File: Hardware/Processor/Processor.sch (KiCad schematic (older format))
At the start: 101 parts, among them J1 5V, J2 UART0, J3 USB_OTG, J4 JTAGICE3-SWD, J5 PIOA, J6 PIOB, J7 PIOC, J8 PIOD, Q1 BSSB06NE, Q2 BSSB06NE, Q3 BSSB06NE, Q4 BSSB06NE, SW1 PB, SW2 PB, SW3 ~RST, U1 TXS0102, U2 ATSAM4E16E, U3 3.0V, U4 LM3671, U5 PRTR5V0U2X, Y1 32.768kHz, Y2 12MHz

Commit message: Added note
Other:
- note added: "Remove local KiCad Libs from past projects"
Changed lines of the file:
@@
 LIBS:valves
 LIBS:common
+LIBS:newFritzLib
 LIBS:Processor-cache
 EELAYER 26 0
@@
 Wire Wire Line
 	9225 9125 9225 9100
+Text Notes 1450 -325 0    394  ~ 0
+Remove local KiCad Libs from past projects
 $EndSCHEMATC

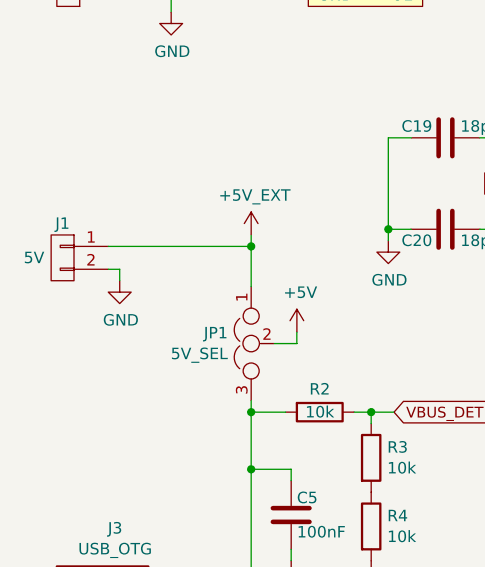
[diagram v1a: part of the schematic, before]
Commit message: Added extra pin to J1 connector to make it surface mount, BOM Complete except for xtals.
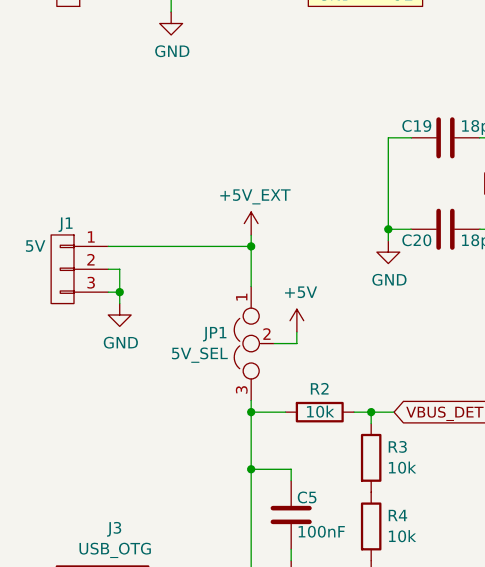
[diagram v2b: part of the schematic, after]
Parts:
- removed J1: 5V, symbol CONN_01X02
- added J1: 5V, symbol CONN_01X03
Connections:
- net +5V_EXT: now also J1.1 (P1)
- net GND: now also J1.2 (P2), J1.3 (P3)
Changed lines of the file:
@@
-$EndComp
-$Comp
-L CONN_01X02 J1
-U 1 1 58AC4E21
-P 925 6875
-F 0 "J1" H 925 7025 50  0000 C CNN
-F 1 "5V" H 1050 6875 50  0000 C CNN
-F 2 "" H -525 -575 50  0001 C CNN
-F 3 "" H -525 -575 50  0001 C CNN
-	1    925  6875
-	-1   0    0    -1
 $EndComp
 $Comp
 L GND #PWR057
 U 1 1 58AC6385
-P 1175 6975
-F 0 "#PWR057" H -875 -75 50  0001 C CNN
-F 1 "GND" H 1180 6802 50  0000 C CNN
-F 2 "" H -875 175 50  0001 C CNN
-F 3 "" H -875 175 50  0001 C CNN
-	1    1175 6975
+P 1175 7075
+F 0 "#PWR057" H -875 25  50  0001 C CNN
+F 1 "GND" H 1180 6902 50  0000 C CNN
+F 2 "" H -875 275 50  0001 C CNN
+F 3 "" H -875 275 50  0001 C CNN
+	1    1175 7075
 	1    0    0    -1
 $EndComp
@@
 	1125 6925 1175 6925
 Wire Wire Line
-	1175 6925 1175 6975
+	1175 6925 1175 7075
 Wire Wire Line
 	1125 6825 1750 6825
@@
 Text Notes 1450 -325 0    394  ~ 0
 Remove local KiCad Libs from past projects
+$Comp
+L CONN_01X03 J1
+U 1 1 58A68985
+P 925 6925
+F 0 "J1" H 875 7125 50  0000 L CNN
+F 1 "5V" H 1000 7025 50  0000 L CNN
+F 2 "" H 75  -300 50  0001 C CNN
+F 3 "" H 75  -300 50  0001 C CNN
+	1    925  6925
+	-1   0    0    -1
+$EndComp
+Wire Wire Line
+	1175 7025 1125 7025
+Connection ~ 1175 7025
 $EndSCHEMATC

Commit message: Fixed some autosave issues
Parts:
- C1, C10, C11, C12, C13, C14, C15, C16, C17, C18, C19, C2, C20, C21, C22, C23, C24, C25, C26, C27, C28, C29, C3, C30, C32, C33, C36, C37, C38, C39, C4, C5, C6, C7, C8, C9, R1, R10, R11, R12, R13, R15, R16, R18, R2, R20, R3, R4, R5, R6, R7, R8, R9: footprint (none) -> Capacitors_SMD:C_0603
- C31, C34, C35, C40, C41, R14, R17, R19, R21, R22: footprint (none) -> Capacitors_SMD:C_0805
- D1, D2, D3, D4, D5: footprint (none) -> LEDs:LED_0805
- J3: footprint (none) -> FritzLib:conn_usb_B_micro_smd
- J5, J7, J8: footprint (none) -> FritzLib:ConnectorSMD-40
- J6: footprint (none) -> FritzLib:ConnectorSMD-24
- SW1, SW2, SW3: footprint (none) -> Buttons_Switches_SMD:SW_SPST_TL3342
- TP1, TP2, TP3, TP4, TP5, TP6, TP7, TP8: footprint (none) -> Measurement_Points:Measurement_Point_Round-SMD-Pad_Small
- U2: footprint (none) -> Housings_QFP:TQFP-144_20x20mm_Pitch0.5mm

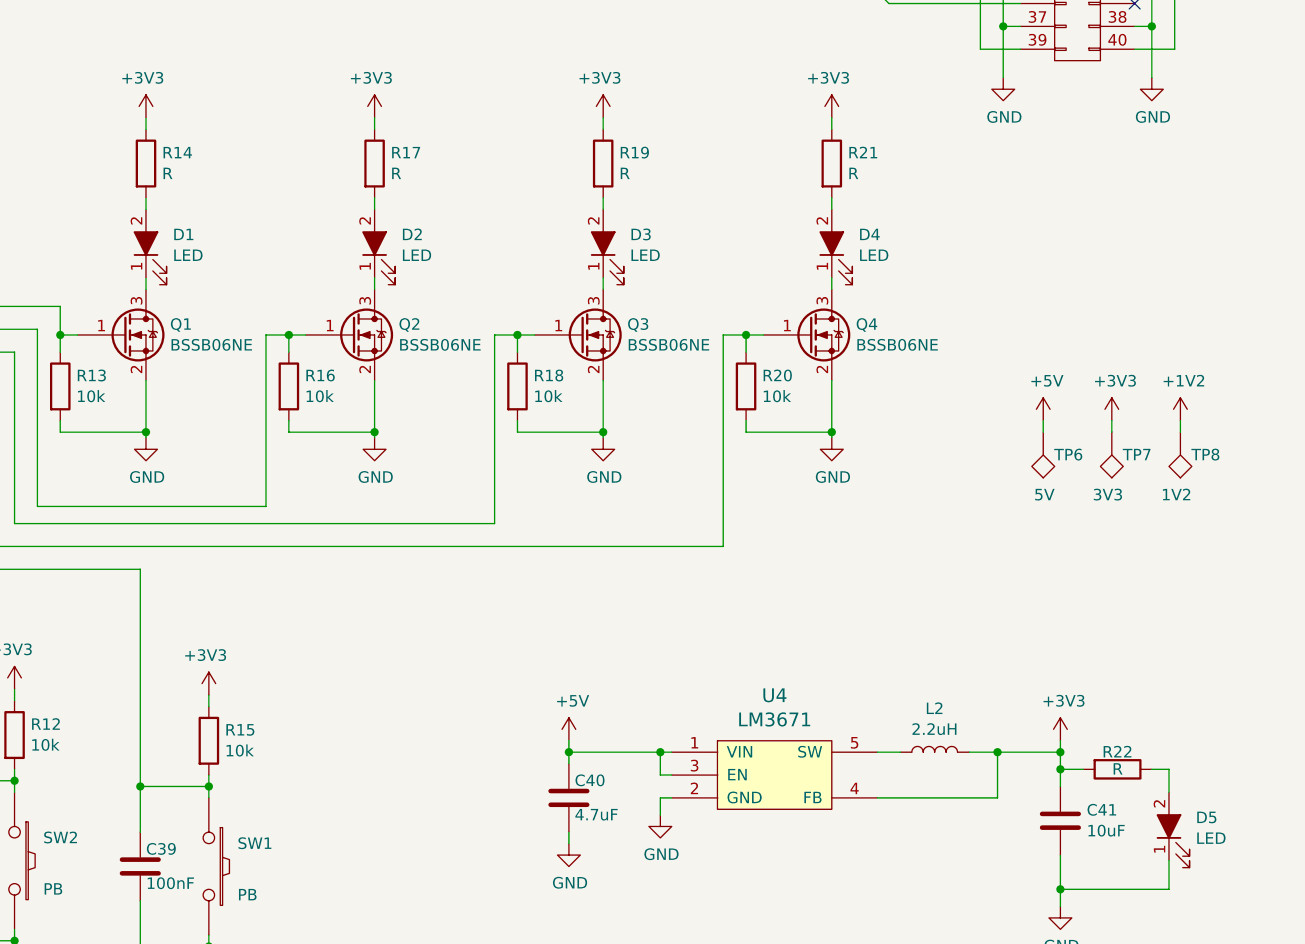
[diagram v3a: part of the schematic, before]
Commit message: Assigned proper value to current limiting resistors for LEDs, fixed autosave file
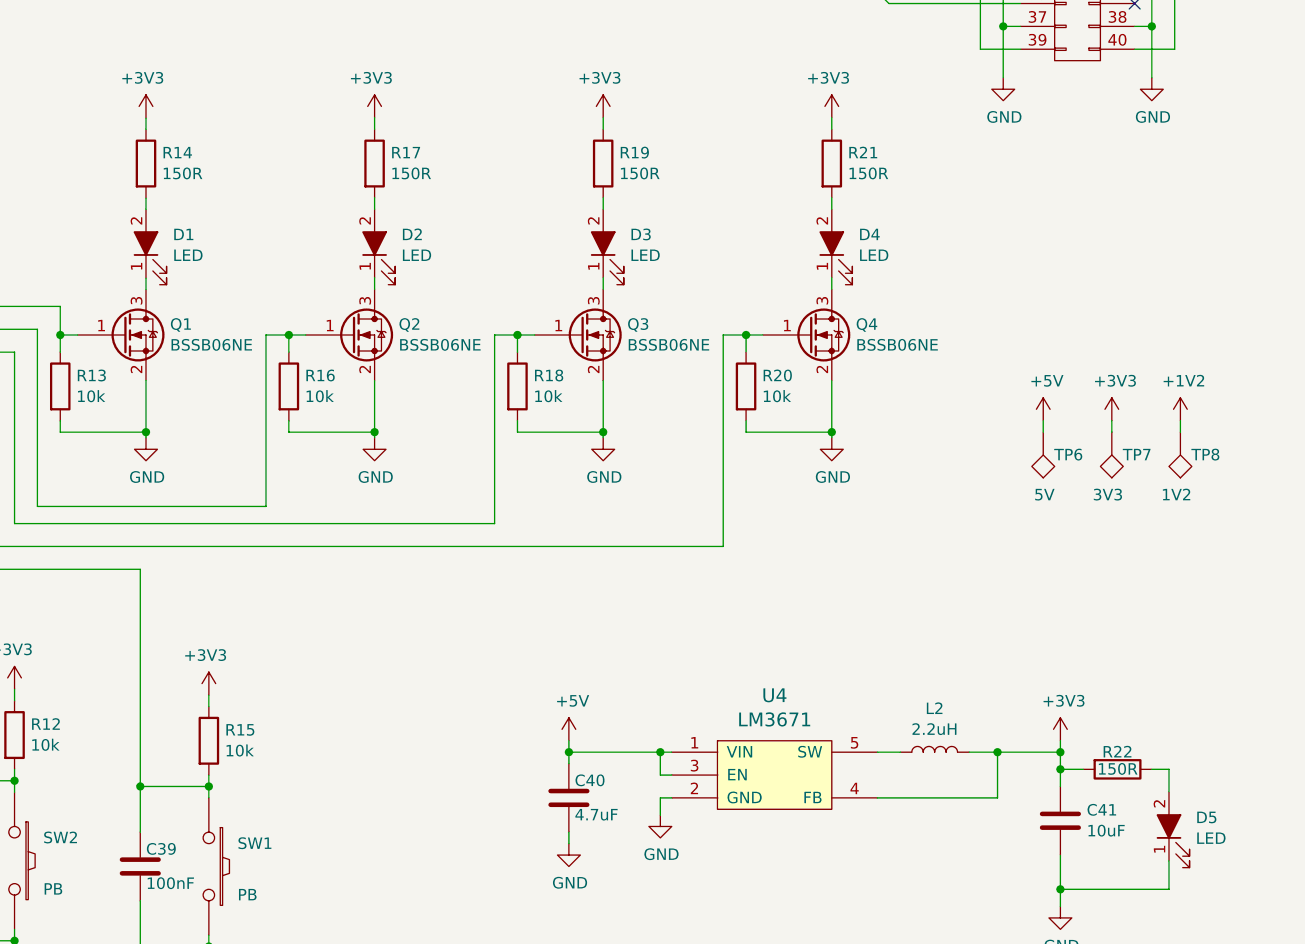
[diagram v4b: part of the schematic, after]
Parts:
- R14, R17, R19, R21, R22: value R -> 150R
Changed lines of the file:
@@
 P 10800 6725
 F 0 "R14" H 10870 6771 50  0000 L CNN
-F 1 "R" H 10870 6680 50  0000 L CNN
+F 1 "150R" H 10870 6680 50  0000 L CNN
 F 2 "Capacitors_SMD:C_0805" V 2705 4775 50  0001 C CNN
 F 3 "" H 2775 4775 50  0001 C CNN
@@
 P 15050 9375
 F 0 "R22" V 14975 9375 50  0000 C CNN
-F 1 "R" V 15050 9375 50  0000 C CNN
+F 1 "150R" V 15050 9375 50  0000 C CNN
 F 2 "Capacitors_SMD:C_0805" V 6955 7425 50  0001 C CNN
 F 3 "" H 7025 7425 50  0001 C CNN
@@
 P 11800 6725
 F 0 "R17" H 11870 6771 50  0000 L CNN
-F 1 "R" H 11870 6680 50  0000 L CNN
+F 1 "150R" H 11870 6680 50  0000 L CNN
 F 2 "Capacitors_SMD:C_0805" V 3705 4775 50  0001 C CNN
 F 3 "" H 3775 4775 50  0001 C CNN
@@
 P 12800 6725
 F 0 "R19" H 12870 6771 50  0000 L CNN
-F 1 "R" H 12870 6680 50  0000 L CNN
+F 1 "150R" H 12870 6680 50  0000 L CNN
 F 2 "Capacitors_SMD:C_0805" V 4705 4775 50  0001 C CNN
 F 3 "" H 4775 4775 50  0001 C CNN
@@
 P 13800 6725
 F 0 "R21" H 13870 6771 50  0000 L CNN
-F 1 "R" H 13870 6680 50  0000 L CNN
+F 1 "150R" H 13870 6680 50  0000 L CNN
 F 2 "Capacitors_SMD:C_0805" V 5705 4775 50  0001 C CNN
 F 3 "" H 5775 4775 50  0001 C CNN

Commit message: Updated BOM & Netlist. Started PCB Layout
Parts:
- J1, JP1: footprint (none) -> FritzLib:ConnectorSMD-1x3
- J2: footprint (none) -> FritzLib:ConnectorSMD-1x4
- J4: footprint (none) -> FritzLib:ConnectorMicromatch-10
- L1: footprint (none) -> FritzLib:Inductor_3mmx3mm
- L2: footprint (none) -> Inductors:Inductor_1212
- Q1, Q2, Q3, Q4, U3: footprint (none) -> TO_SOT_Packages_SMD:SOT-23
- U1: footprint (none) -> Housings_SSOP:MSOP-8_3x3mm_Pitch0.65mm
- U4: footprint (none) -> TO_SOT_Packages_SMD:SOT-23-5
- U5: footprint (none) -> FritzLib:SOT143B
- Y1: footprint (none) -> FritzLib:FC-135R
- Y2: footprint (none) -> Crystals:Crystal_HC49-SD_SMD
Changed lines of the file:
@@
 F 0 "L2" V 14440 9300 50  0000 C CNN
 F 1 "2.2uH" V 14349 9300 50  0000 C CNN
-F 2 "" H 4000 4725 50  0001 C CNN
+F 2 "Inductors:Inductor_1212" H 4000 4725 50  0001 C CNN
 F 3 "" H 4000 4725 50  0001 C CNN
 	1    14250 9300
@@
 F 0 "L1" H 5984 1704 50  0000 R CNN
 F 1 "10uH" H 5984 1795 50  0000 R CNN
-F 2 "" H -4225 -2825 50  0001 C CNN
+F 2 "FritzLib:Inductor_3mmx3mm" H -4225 -2825 50  0001 C CNN
 F 3 "" H -4225 -2825 50  0001 C CNN
 	1    6025 1750
@@
 F 0 "U3" V 7054 2554 50  0000 L CNN
 F 1 "3.0V" V 7145 2554 50  0000 L CNN
-F 2 "" H -4025 100 50  0001 C CNN
+F 2 "TO_SOT_Packages_SMD:SOT-23" H -4025 100 50  0001 C CNN
 F 3 "" H -4025 100 50  0001 C CNN
 F 4 "LM4040C30" V 7100 2475 60  0001 C CNN "MFG#"
@@
 F 0 "J4" H 10100 2665 50  0000 C CNN
 F 1 "JTAGICE3-SWD" H 10100 2574 50  0000 C CNN
-F 2 "" H -3175 -3425 50  0001 C CNN
+F 2 "FritzLib:ConnectorMicromatch-10" H -3175 -3425 50  0001 C CNN
 F 3 "" H -3175 -3425 50  0001 C CNN
 	1    10100 2250
@@
 F 0 "U4" H 13550 9847 60  0000 C CNN
 F 1 "LM3671" H 13550 9741 60  0000 C CNN
-F 2 "" H 11900 10750 60  0001 C CNN
+F 2 "TO_SOT_Packages_SMD:SOT-23-5" H 11900 10750 60  0001 C CNN
 F 3 "" H 11900 10750 60  0001 C CNN
 	1    13550 9450
@@
 F 0 "U5" H 2525 9497 60  0000 C CNN
 F 1 "PRTR5V0U2X" H 2525 9391 60  0000 C CNN
-F 2 "" H -1175 3525 60  0001 C CNN
+F 2 "FritzLib:SOT143B" H -1175 3525 60  0001 C CNN
 F 3 "" H -1175 3525 60  0001 C CNN
 	1    2525 9200
@@
 F 0 "Q1" H 10905 7521 50  0000 L CNN
 F 1 "BSSB06NE" H 10905 7430 50  0000 L CNN
-F 2 "" H -425 -625 50  0001 C CNN
+F 2 "TO_SOT_Packages_SMD:SOT-23" H -425 -625 50  0001 C CNN
 F 3 "" H -625 -725 50  0001 C CNN
 	1    10700 7475
@@
 F 0 "Q2" H 11905 7521 50  0000 L CNN
 F 1 "BSSB06NE" H 11905 7430 50  0000 L CNN
-F 2 "" H 575 -625 50  0001 C CNN
+F 2 "TO_SOT_Packages_SMD:SOT-23" H 575 -625 50  0001 C CNN
 F 3 "" H 375 -725 50  0001 C CNN
 	1    11700 7475
@@
 F 0 "Q3" H 12905 7521 50  0000 L CNN
 F 1 "BSSB06NE" H 12905 7430 50  0000 L CNN
-F 2 "" H 1575 -625 50  0001 C CNN
+F 2 "TO_SOT_Packages_SMD:SOT-23" H 1575 -625 50  0001 C CNN
 F 3 "" H 1375 -725 50  0001 C CNN
 	1    12700 7475
@@
 F 0 "Y2" V 2829 6681 50  0000 L CNN
 F 1 "12MHz" V 2920 6681 50  0000 L CNN
-F 2 "" H -725 -300 50  0001 C CNN
+F 2 "Crystals:Crystal_HC49-SD_SMD" H -725 -300 50  0001 C CNN
 F 3 "" H -725 -300 50  0001 C CNN
 	1    2875 6550
@@
 F 0 "Y1" V 2654 3931 50  0000 L CNN
 F 1 "32.768kHz" V 2745 3931 50  0000 L CNN
-F 2 "" H -900 -3050 50  0001 C CNN
+F 2 "FritzLib:FC-135R" H -900 -3050 50  0001 C CNN
 F 3 "" H -900 -3050 50  0001 C CNN
 	1    2700 3800
@@
 F 0 "U1" H 2250 5944 47  0000 C CNN
 F 1 "TXS0102" H 2250 5857 47  0000 C CNN
-F 2 "" H -700 800 47  0001 C CNN
+F 2 "Housings_SSOP:MSOP-8_3x3mm_Pitch0.65mm" H -700 800 47  0001 C CNN
 F 3 "" H -700 800 47  0001 C CNN
 	1    2250 5575
@@
 F 0 "J2" H 950 5250 50  0000 C CNN
 F 1 "UART0" H 950 5325 50  0000 C CNN
-F 2 "" H -475 225 50  0001 C CNN
+F 2 "FritzLib:ConnectorSMD-1x4" H -475 225 50  0001 C CNN
 F 3 "" H -475 225 50  0001 C CNN
 	1    950  5575
@@
 F 0 "JP1" V 1704 7352 50  0000 L CNN
 F 1 "5V_SEL" V 1795 7352 50  0000 L CNN
-F 2 "" H -200 -400 50  0001 C CNN
+F 2 "FritzLib:ConnectorSMD-1x3" H -200 -400 50  0001 C CNN
 F 3 "" H -200 -400 50  0001 C CNN
 	1    1750 7250
@@
 F 0 "Q4" H 13905 7521 50  0000 L CNN
 F 1 "BSSB06NE" H 13905 7430 50  0000 L CNN
-F 2 "" H 2575 -625 50  0001 C CNN
+F 2 "TO_SOT_Packages_SMD:SOT-23" H 2575 -625 50  0001 C CNN
 F 3 "" H 2375 -725 50  0001 C CNN
 	1    13700 7475
@@
 F 0 "J1" H 875 7125 50  0000 L CNN
 F 1 "5V" H 1000 7025 50  0000 L CNN
-F 2 "" H 75  -300 50  0001 C CNN
+F 2 "FritzLib:ConnectorSMD-1x3" H 75  -300 50  0001 C CNN
 F 3 "" H 75  -300 50  0001 C CNN
 	1    925  6925

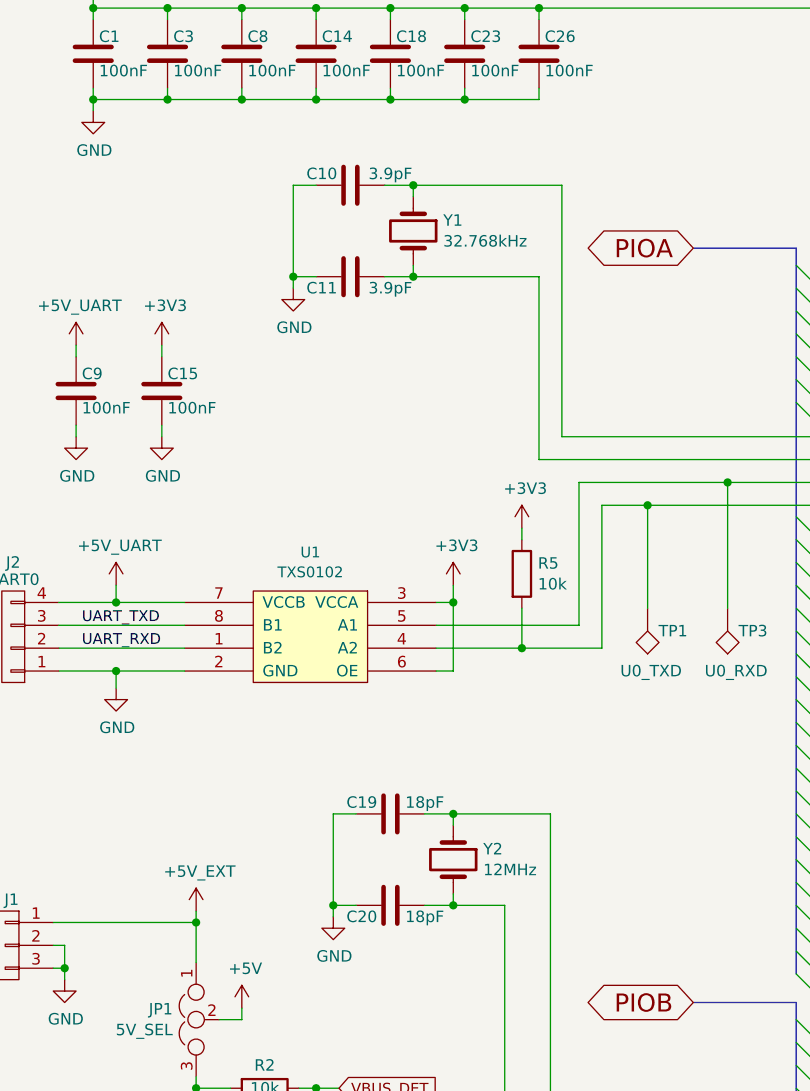
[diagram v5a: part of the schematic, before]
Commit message: Removed backup files. Updated values of xtal ext caps
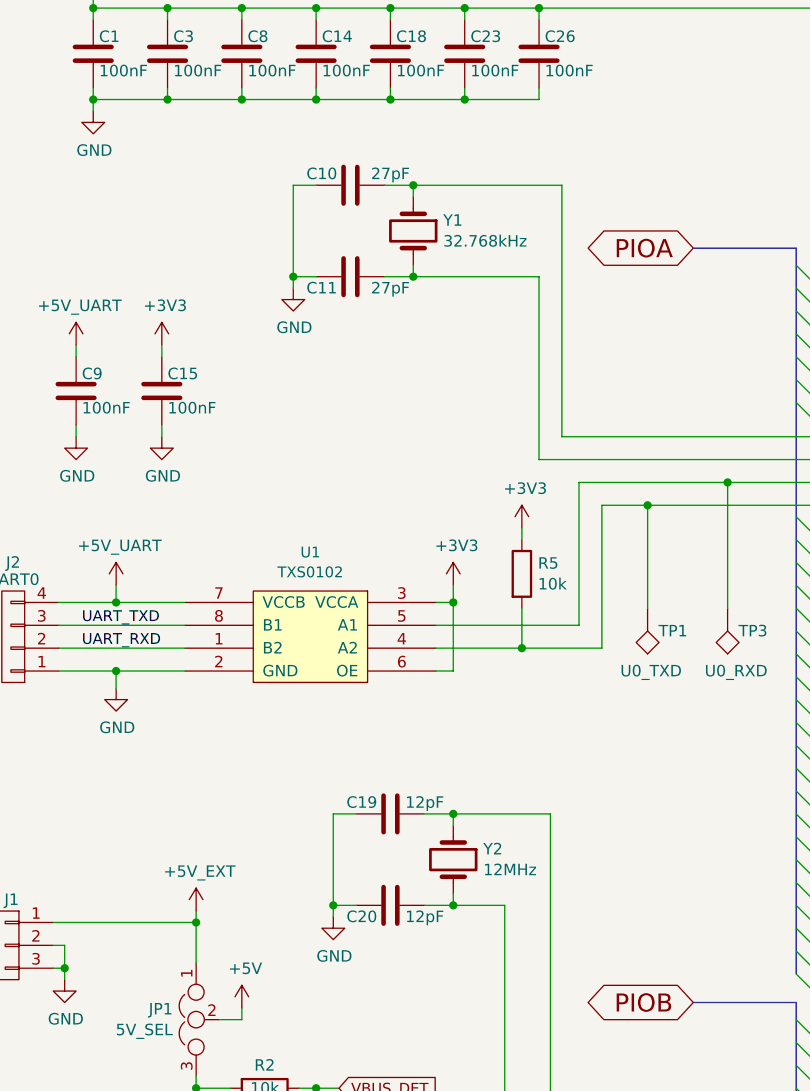
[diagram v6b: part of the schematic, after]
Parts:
- C10, C11: value 3.9pF -> 27pF
- C19, C20: value 18pF -> 12pF
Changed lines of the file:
@@
 P 2600 6350
 F 0 "C19" V 2550 6225 50  0000 C CNN
-F 1 "18pF" V 2550 6500 50  0000 C CNN
+F 1 "12pF" V 2550 6500 50  0000 C CNN
 F 2 "Capacitors_SMD:C_0603" H -337 -650 50  0001 C CNN
 F 3 "" H -375 -500 50  0001 C CNN
@@
 P 2600 6750
 F 0 "C20" V 2650 6625 50  0000 C CNN
-F 1 "18pF" V 2650 6900 50  0000 C CNN
+F 1 "12pF" V 2650 6900 50  0000 C CNN
 F 2 "Capacitors_SMD:C_0603" H -337 -250 50  0001 C CNN
 F 3 "" H -375 -100 50  0001 C CNN
@@
 P 2425 3600
 F 0 "C10" V 2375 3475 50  0000 C CNN
-F 1 "3.9pF" V 2375 3775 50  0000 C CNN
+F 1 "27pF" V 2375 3775 50  0000 C CNN
 F 2 "Capacitors_SMD:C_0603" H -512 -3400 50  0001 C CNN
 F 3 "" H -550 -3250 50  0001 C CNN
@@
 P 2425 4000
 F 0 "C11" V 2475 3875 50  0000 C CNN
-F 1 "3.9pF" V 2475 4175 50  0000 C CNN
+F 1 "27pF" V 2475 4175 50  0000 C CNN
 F 2 "Capacitors_SMD:C_0603" H -512 -3000 50  0001 C CNN
 F 3 "" H -550 -2850 50  0001 C CNN
